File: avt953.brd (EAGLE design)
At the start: 100 x 80 mm, 51 parts, among them CON3 RJ45-6L2-B, CON4A MKDS_5/3-6,35, CON4B MKDS_5/3-6,35, CON4C MKDS_5/3-6,35, CON4D MKDS_5/3-6,35, X1 20MHz, X2 20MHz

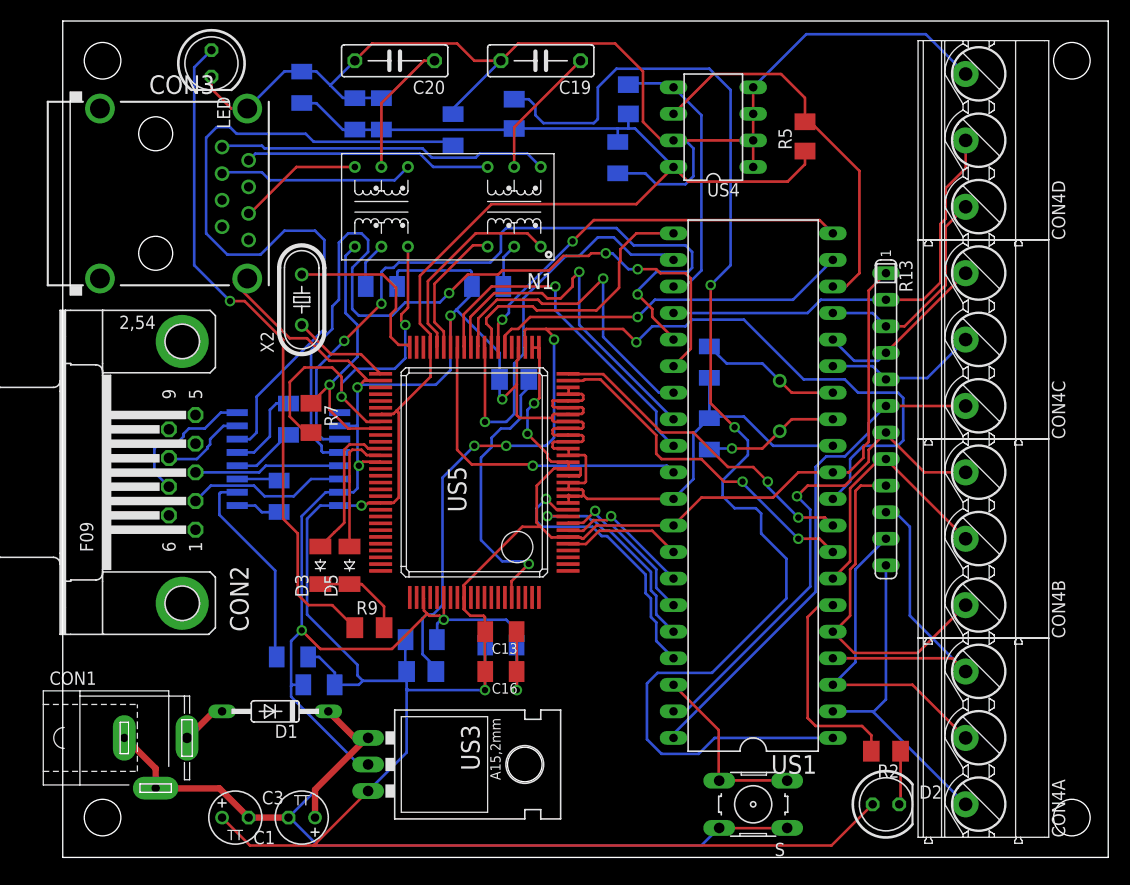
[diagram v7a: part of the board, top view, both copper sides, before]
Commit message: Oblano warstwy top i bottom masą. Uzupełniono przelotki.
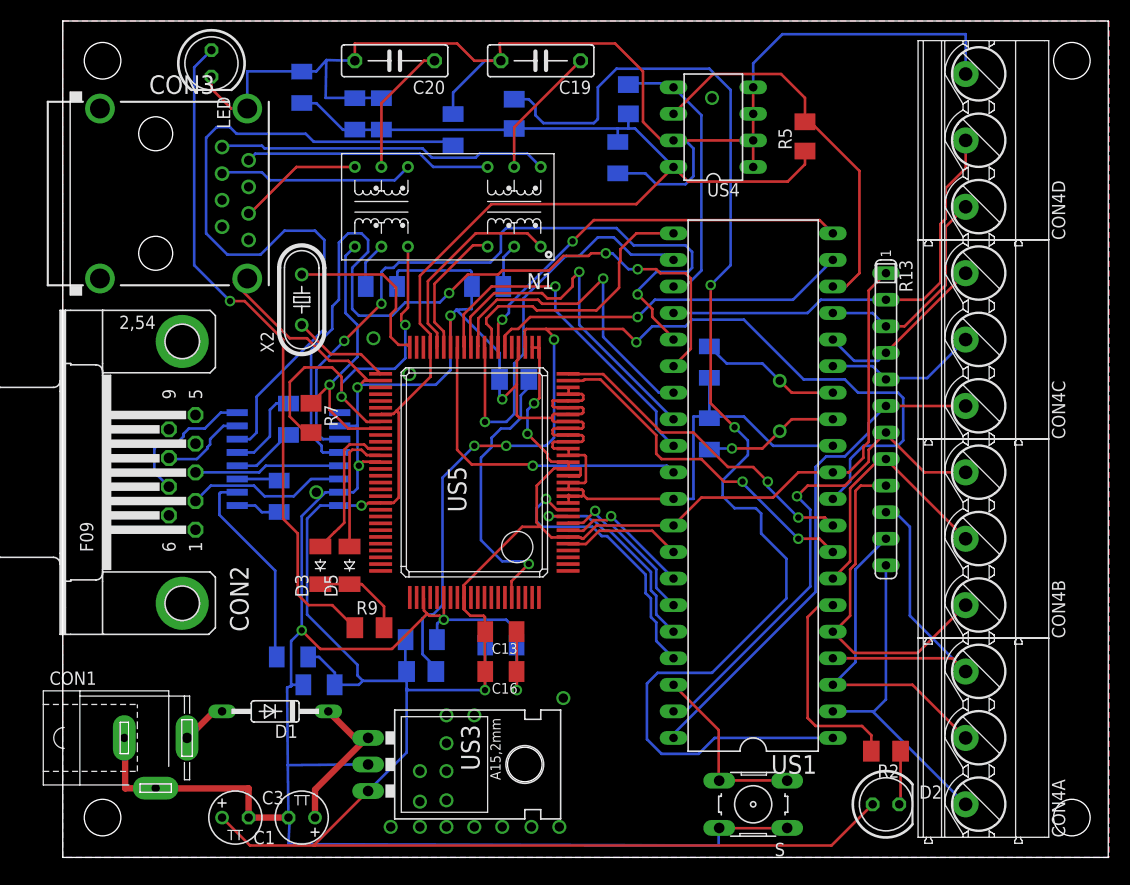
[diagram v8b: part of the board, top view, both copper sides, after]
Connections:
- net GND: now also CON2.5
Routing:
- net GND: track 442.3 -> 462.6 mm, vias 7 -> 26
- added copper zone on layer 1, net GND
- added copper zone on layer 16, net GND
